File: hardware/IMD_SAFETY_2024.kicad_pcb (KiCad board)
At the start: 4 copper layers, 66.8 x 60 mm, 99 parts, among them J1 Main- M80-5000842, K2 TE AXICOM IM07DTS, Q1 2N7002, U1 LM393, U10 74HCS08, U13 74HC74, U14 LM393, U15 LM393, U16 LM393, U2 74AC04SC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

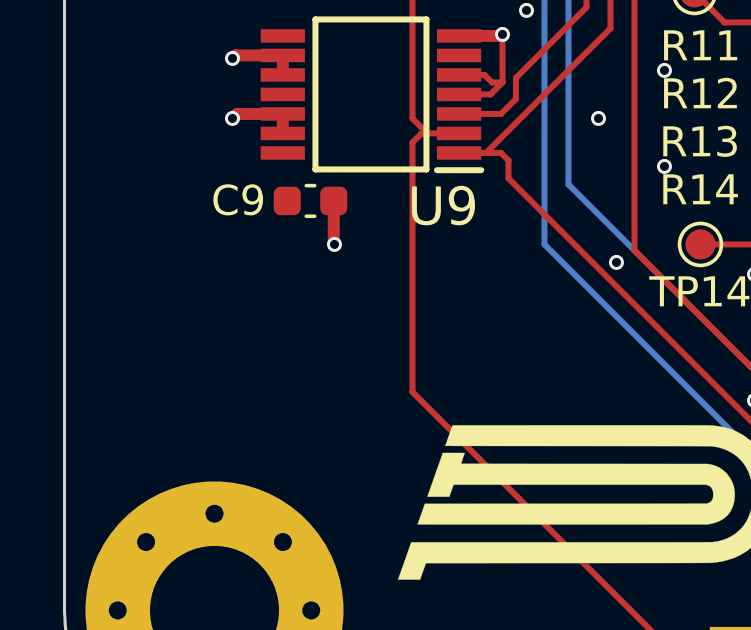
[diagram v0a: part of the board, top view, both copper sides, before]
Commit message: Add 0V jumper
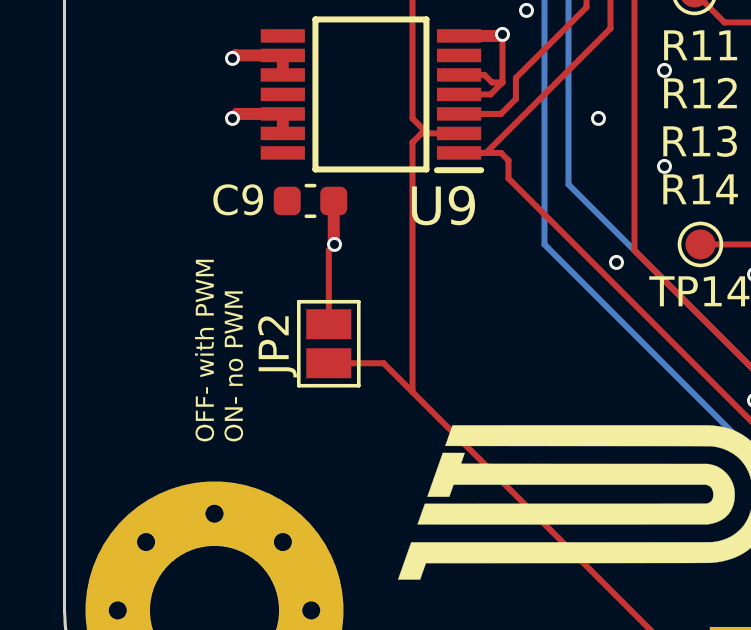
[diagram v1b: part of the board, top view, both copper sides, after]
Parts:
- added JP2: Bender_NoUndervolt, Jumper:SolderJumper-2_P1.3mm_Open_Pad1.0x1.5mm, F.Cu at (119.8, 107.1)
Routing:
- net /DUTY&FREQ_OK: track 51.9 -> 55.1 mm
- net GND: track 113.0 -> 115.8 mm
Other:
- board text added: "OFF- with PWM ON- no PWM"
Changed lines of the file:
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@@
 		)
 	)
+	(footprint "Jumper:SolderJumper-2_P1.3mm_Open_Pad1.0x1.5mm"
+		(layer "F.Cu")
+		(at 119.81 107.11 90)
+		(descr "SMD Solder Jumper, 1x1.5mm Pads, 0.3mm gap, open")
+		(tags "solder jumper open")
+		(property "Reference" "JP2"
+			(at 0 -1.8 -90)
+			(layer "F.SilkS")
+			(effects
+				(font
+					(size 1 1)
+					(thickness 0.15)
+				)
+			)
+		)
+		(property "Value" "Bender_NoUndervolt"
+			(at 0 1.9 -90)
+			(layer "F.Fab")
+			(effects
+				(font
+					(size 1 1)
+					(thickness 0.15)
+				)
+			)
+		)
+		(property "Footprint" "Jumper:SolderJumper-2_P1.3mm_Open_Pad1.0x1.5mm"
+			(at 0 0 90)
+			(unlocked yes)
+			(layer "F.Fab")
+			(hide yes)
+			(effects
+				(font
+					(size 1.27 1.27)
+				)
+			)
+		)
+		(property "Datasheet" ""
+			(at 0 0 90)
+			(unlocked yes)
+			(layer "F.Fab")
+			(hide yes)
+			(effects
+				(font
+					(size 1.27 1.27)
+				)
+			)
+		)
+		(property "Description" "Solder Jumper, 2-pole, open"
+			(at 0 0 90)
+			(unlocked yes)
+			(layer "F.Fab")
+			(hide yes)
+			(effects
+				(font
+					(size 1.27 1.27)
+				)
+			)
+		)
+		(property "Mouser#" ""
+			(at 0 0 90)
+			(unlocked yes)
+			(layer "F.Fab")
+			(hide yes)
+			(effects
+				(font
+					(size 0.8 0.8)
+					(thickness 0.1)
+				)
+			)
+		)
+		(property "TME#" ""
+			(at 0 0 90)
+			(unlocked yes)
+			(layer "F.Fab")
+			(hide yes)
+			(effects
+				(font
+					(size 0.8 0.8)
+					(thickness 0.1)
+				)
+			)
+		)
+		(property ki_fp_filters "SolderJumper*Open*")
+		(sheetname "Root")
+		(sheetfile "IMD_SAFETY_2024.kicad_sch")
+		(zone_connect 1)
+		(attr exclude_from_pos_files)
+		(fp_line
+			(start 1.4 -1)
+			(end 1.4 1)
+			(stroke
+				(width 0.12)
+				(type solid)
+			)
+			(layer "F.SilkS")
+		)
+		(fp_line
+			(start -1.4 -1)
+			(end 1.4 -1)
+			(stroke
+				(width 0.12)
+				(type solid)
+			)
+			(layer "F.SilkS")
+		)
+		(fp_line
+			(start 1.4 1)
+			(end -1.4 1)
+			(stroke
+				(width 0.12)
+				(type solid)
+			)
+			(layer "F.SilkS")
+		)
+		(fp_line
+			(start -1.4 1)
+			(end -1.4 -1)
+			(stroke
+				(width 0.12)
+				(type solid)
+			)
+			(layer "F.SilkS")
+		)
+		(fp_line
+			(start -1.65 -1.25)
+			(end 1.65 -1.25)
+			(stroke
+				(width 0.05)
+				(type solid)
+			)
+			(layer "F.CrtYd")
+		)
+		(fp_line
+			(start -1.65 -1.25)
+			(end -1.65 1.25)
+			(stroke
+				(width 0.05)
+				(type solid)
+			)
+			(layer "F.CrtYd")
+		)
+		(fp_line
+			(start 1.65 1.25)
+			(end 1.65 -1.25)
+			(stroke
+				(width 0.05)
+				(type solid)
+			)
+			(layer "F.CrtYd")
+		)
+		(fp_line
+			(start 1.65 1.25)
+			(end -1.65 1.25)
+			(stroke
+				(width 0.05)
+				(type solid)
+			)
+			(layer "F.CrtYd")
+		)
+		(pad "1" smd rect
+			(at -0.649999 0 90)
+			(size 1 1.5)
+			(layers "F.Cu" "F.Mask")
+			(net 41 "/DUTY&FREQ_OK")
+			(pinfunction "A")
+			(pintype "passive")
+		)
+		(pad "2" smd rect
+			(at 0.649999 0 90)
+			(size 1 1.5)
+			(layers "F.Cu" "F.Mask")
+			(net 2 "GND")
+			(pinfunction "B")
+			(pintype "passive")
+		)
+	)
 	(footprint "Resistor_SMD:R_0603_1608Metric"
 		(layer "F.Cu")
@@
 		)
 	)
+	(gr_text "OFF- with PWM\nON- no PWM\n"
+		(at 117.016 110.412 90)
+		(layer "F.SilkS")
+		(effects
+			(font
+				(size 0.6 0.6)
+				(thickness 0.1)
+			)
+			(justify left bottom)
+		)
+	)
 	(gr_text "Logic analyzer test points"
 		(at 135.4 120.4 0)
@@
 	)
 	(segment
+		(start 119.81 103.99)
+		(end 120 103.8)
+		(width 0.2)
+		(layer "F.Cu")
+		(net 2)
+	)
+	(segment
 		(start 168.511999 70.788)
 		(end 169.086 70.788)
@@
 	)
 	(segment
+		(start 119.81 106.460001)
+		(end 119.81 103.99)
+		(width 0.2)
+		(layer "F.Cu")
+		(net 2)
+	)
+	(segment
 		(start 125.6 90.8)
 		(end 125.35 90.55)
@@
 		(width 0.2)
 		(layer "F.Cu")
+		(net 41)
+	)
+	(segment
+		(start 121.639999 107.759999)
+		(end 122.6 108.72)
+		(width 0.2)
+		(layer "F.Cu")
+		(net 41)
+	)
+	(segment
+		(start 119.81 107.759999)
+		(end 121.639999 107.759999)
+		(width 0.2)
+		(layer "F.Cu")

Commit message: Add input stage LM393 comment
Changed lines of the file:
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@@
 			(size 1.025 1.4)
 			(layers "F.Cu" "F.Paste" "F.Mask")
-			(roundrect_rratio 0.243902)
+			(roundrect_rratio 0.243902439)
 			(net 15 "COCKPIT_LED")
 			(pintype "passive")
@@
 			(size 1.025 1.4)
 			(layers "F.Cu" "F.Paste" "F.Mask")
-			(roundrect_rratio 0.243902)
+			(roundrect_rratio 0.243902439)
 			(net 20 "Net-(K2-Pad4)")
 			(pintype "passive")
@@
 			(size 1.025 1.4)
 			(layers "F.Cu" "F.Paste" "F.Mask")
-			(roundrect_rratio 0.243902)
+			(roundrect_rratio 0.243902439)
 			(net 14 "RESET")
 			(pintype "passive")
@@
 			(size 1.025 1.4)
 			(layers "F.Cu" "F.Paste" "F.Mask")
-			(roundrect_rratio 0.243902)
+			(roundrect_rratio 0.243902439)
 			(net 59 "EXT_RESET")
 			(pintype "passive")
